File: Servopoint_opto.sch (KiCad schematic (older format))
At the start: 29 parts, among them J1 TBP01R1-508-04BE, J2 TBP01R1-508-04BE, J3 Conn_01x05_Male, J5 Servo, J6 TBP01R1-508-03BE, J7 TBP01R1-508-03BE, Q1 BC847, Q2 BC847, U1 6N137, U2 LM2596S-5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

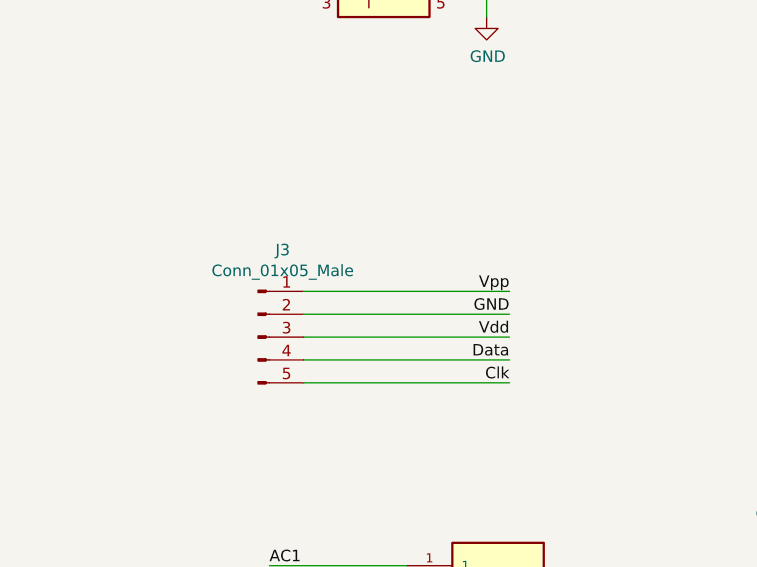
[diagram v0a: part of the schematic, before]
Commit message: changed pcb to 6 pin socket to programm pic via pickit 3, BOM and partnumber not updated yet, pcb not tested yet
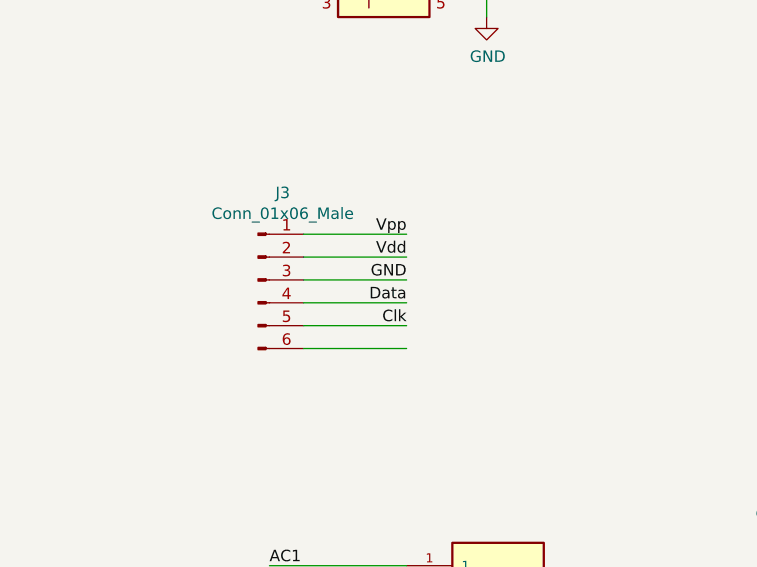
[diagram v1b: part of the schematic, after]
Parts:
- removed J3: Conn_01x05_Male, Connector_PinHeader_2.54mm:PinHeader_1x05_P2.54mm_Vertical, symbol Connector:Conn_01x05_Male
- added J3: Conn_01x06_Male, symbol Connector:Conn_01x06_Male
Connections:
- net Clk: now also J3.5 (Pin_5)
- net Data: now also J3.4 (Pin_4)
- net GND: now also J3.3 (Pin_3)
- net Vdd: now also J3.2 (Pin_2)
- net Vpp: now also J3.1 (Pin_1)
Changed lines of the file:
@@
 	1    0    0    -1
 $EndComp
-$Comp
-L Connector:Conn_01x05_Male J3
-U 1 1 609C52EE
-P 2150 5250
-F 0 "J3" H 2258 5631 50  0000 C CNN
-F 1 "Conn_01x05_Male" H 2258 5540 50  0000 C CNN
-F 2 "Connector_PinHeader_2.54mm:PinHeader_1x05_P2.54mm_Vertical" H 2150 5250 50  0001 C CNN
-F 3 "~" H 2150 5250 50  0001 C CNN
-	1    2150 5250
-	1    0    0    -1
-$EndComp
-Wire Wire Line
-	2350 5050 3250 5050
-Wire Wire Line
-	2350 5150 3250 5150
-Wire Wire Line
-	2350 5250 3250 5250
-Wire Wire Line
-	2350 5350 3250 5350
-Wire Wire Line
-	2350 5450 3250 5450
-Text Label 3250 5050 2    50   ~ 0
-Vpp
-Text Label 3250 5150 2    50   ~ 0
-GND
-Text Label 3250 5250 2    50   ~ 0
-Vdd
-Text Label 3250 5350 2    50   ~ 0
-Data
-Text Label 3250 5450 2    50   ~ 0
-Clk
 Text Label 4900 2250 0    50   ~ 0
 Vdd
@@
 	0    -1   -1   0
 $EndComp
+$Comp
+L Connector:Conn_01x06_Male J3
+U 1 1 615D9BD3
+P 2150 5000
+F 0 "J3" H 2258 5381 50  0000 C CNN
+F 1 "Conn_01x06_Male" H 2258 5290 50  0000 C CNN
+F 2 "" H 2150 5000 50  0001 C CNN
+F 3 "~" H 2150 5000 50  0001 C CNN
+	1    2150 5000
+	1    0    0    -1
+$EndComp
+Wire Wire Line
+	2350 4800 2800 4800
+Wire Wire Line
+	2350 4900 2800 4900
+Wire Wire Line
+	2350 5000 2800 5000
+Wire Wire Line
+	2350 5100 2800 5100
+Wire Wire Line
+	2350 5200 2800 5200
+Wire Wire Line
+	2350 5300 2800 5300
+Text Label 2800 4900 2    50   ~ 0
+Vdd
+Text Label 2800 5000 2    50   ~ 0
+GND
+Text Label 2800 5200 2    50   ~ 0
+Clk
+Text Label 2800 5100 2    50   ~ 0
+Data
+Text Label 2800 4800 2    50   ~ 0
+Vpp
 $EndSCHEMATC
